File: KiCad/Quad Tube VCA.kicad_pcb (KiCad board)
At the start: 2 copper layers, 162.6 x 100.3 mm, 226 parts, among them IC1 TL072, IC10 TL072, IC2 LM358, IC3 TL072, IC4 LM358, IC5 TL072, IC6 LM358, IC7 TL072, IC8 LM358, IC9 TL072

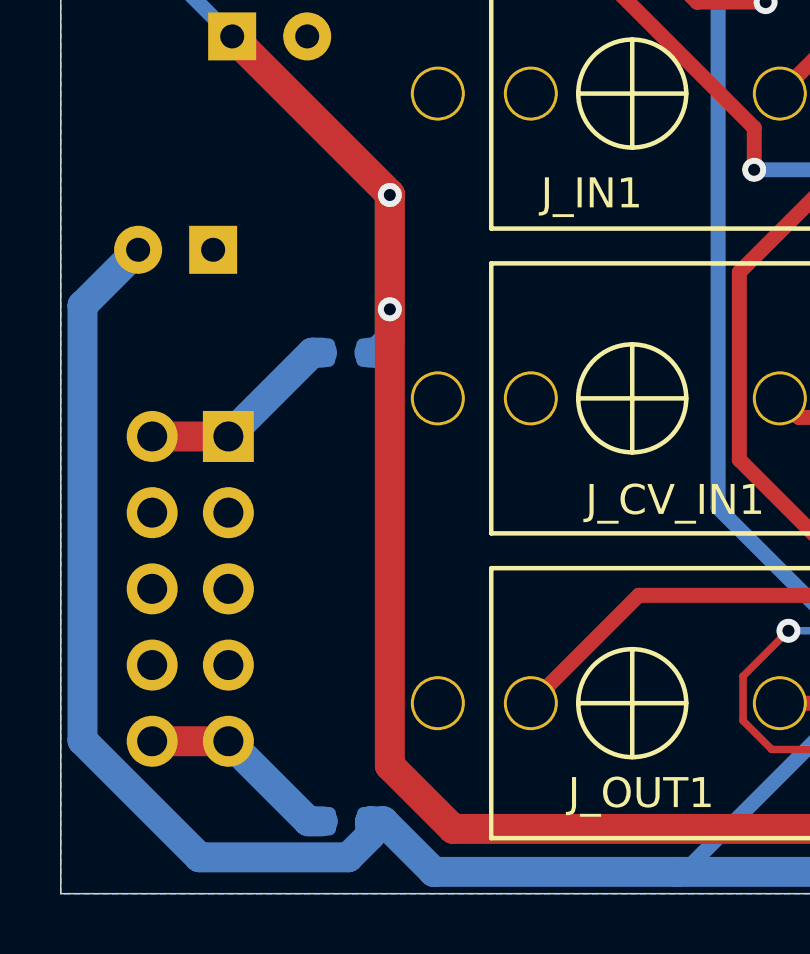
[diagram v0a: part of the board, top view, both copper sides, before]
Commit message: adds reverse power protection diodes
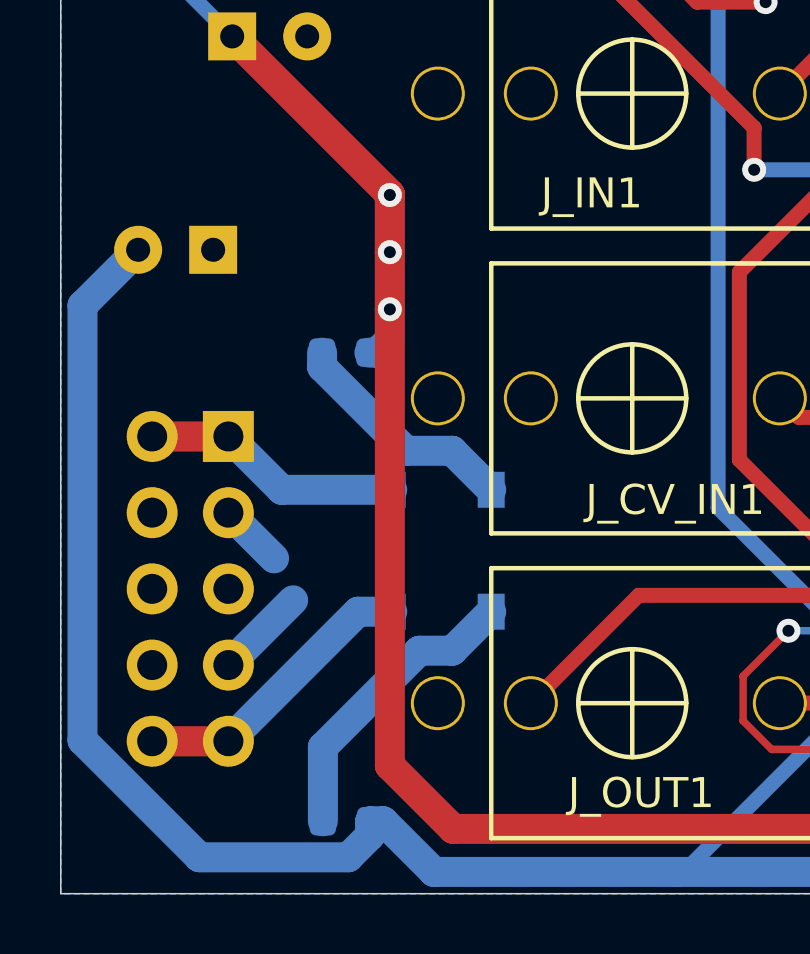
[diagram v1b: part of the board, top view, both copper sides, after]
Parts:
- added D19: 1N5819, Diode_SMD:D_SOD-123, B.Cu at (78.7, 131.3)
- added D20: 1N5819, Diode_SMD:D_SOD-123, B.Cu at (78.7, 135.4)
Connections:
- FB1 pad 1: Net-(FB1-Pad1) -> Net-(D19-Pad1)
- FB2 pad 1: Net-(FB2-Pad1) -> Net-(D20-Pad2)
- JP1 pad 1: Net-(FB1-Pad1) -> Net-(D19-Pad2)
- JP1 pad 10: Net-(FB2-Pad1) -> Net-(D20-Pad1)
- JP1 pad 2: Net-(FB1-Pad1) -> Net-(D19-Pad2)
- JP1 pad 9: Net-(FB2-Pad1) -> Net-(D20-Pad1)
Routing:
- net Net-(D20-Pad2): track 0.00 -> 9.95 mm
- net Net-(D20-Pad1): track 0.00 -> 9.79 mm
- net Net-(D19-Pad2): track 0.00 -> 8.74 mm
- net Net-(D19-Pad1): track 0.00 -> 7.81 mm
- net Net-(FB1-Pad1): track 6.82 -> 0.00 mm
- net Net-(FB2-Pad1): track 6.79 -> 0.00 mm
- net GND: track 383.2 -> 388.5 mm
- net +12V: vias 10 -> 11
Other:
- board text removed: "I’VE GOT THE POWER!!"

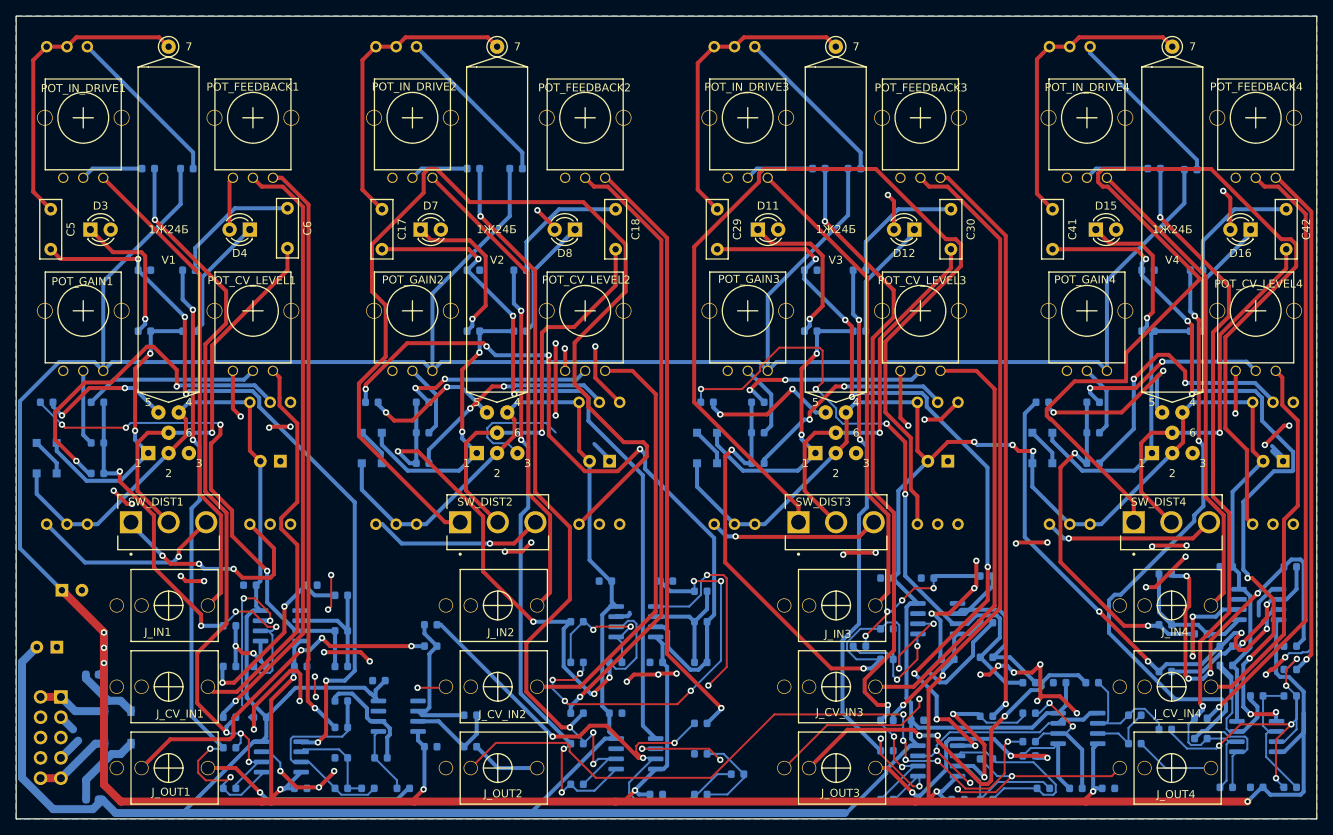
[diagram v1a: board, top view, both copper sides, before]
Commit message: removes leds from cathode/signal path
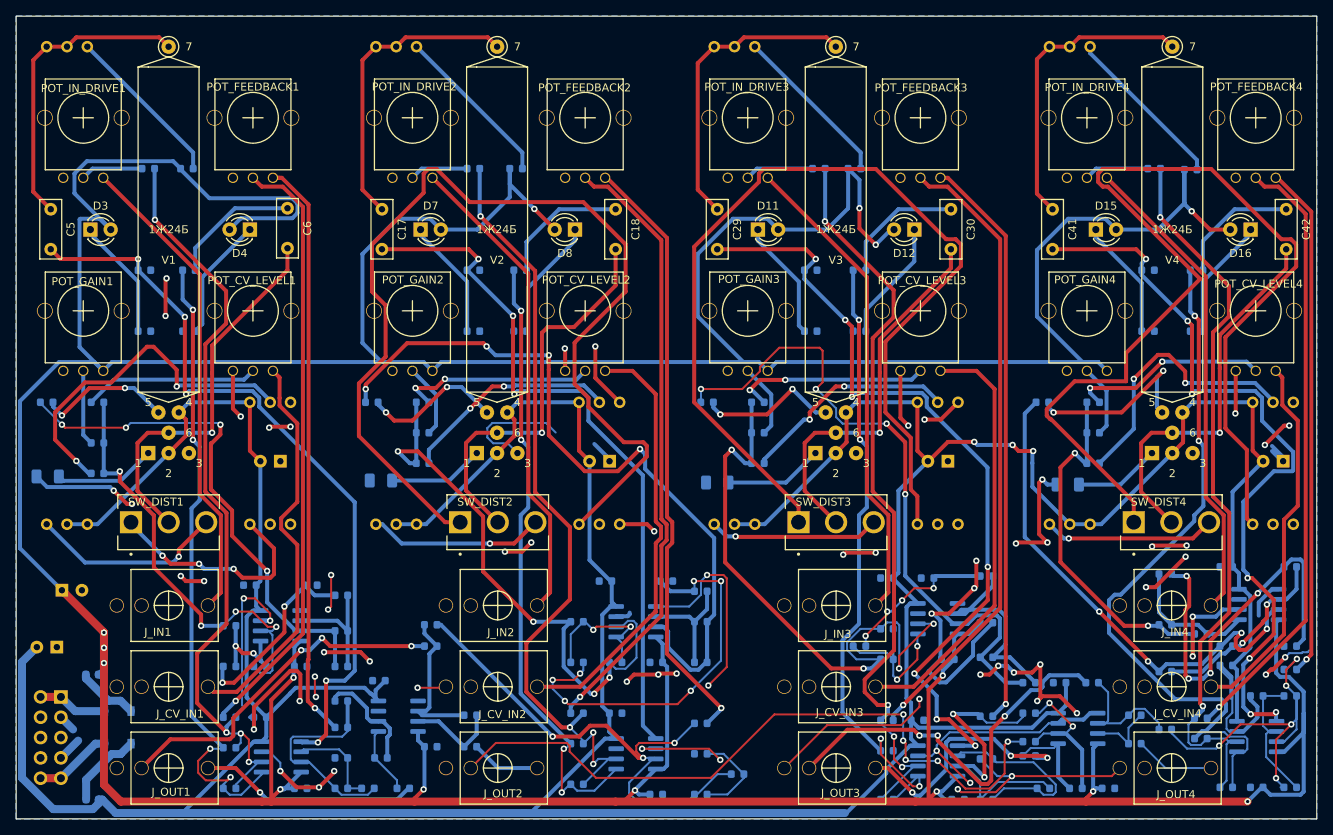
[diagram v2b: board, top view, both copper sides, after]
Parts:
- removed D10, D13, D14, D17, D18, D5, D6, D9: 1n4148, Diode_SMD:D_SOD-323_HandSoldering
- added R92: 750R, Resistor_SMD:R_1206_3216Metric, B.Cu at (70.0, 102.0)
- added R93: 750R, Resistor_SMD:R_1206_3216Metric, B.Cu at (111.6, 102.5)
- added R94: 750R, Resistor_SMD:R_1206_3216Metric, B.Cu at (153.7, 102.7)
- added R95: 750R, Resistor_SMD:R_1206_3216Metric, B.Cu at (197.5, 103.0)
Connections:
- D11 pad 2: GND -> +12V
- D12 pad 2: GND -> +12V
- D15 pad 2: GND -> +12V
- D16 pad 2: GND -> +12V
- D3 pad 2: GND -> +12V
- D4 pad 2: GND -> +12V
- D7 pad 2: GND -> +12V
- D8 pad 2: GND -> +12V
- R11 pad 1: Net-(D5-Pad2) -> GND
- R13 pad 2: Net-(D5-Pad2) -> GND
- R31 pad 1: Net-(D9-Pad2) -> GND
- R33 pad 2: Net-(D9-Pad2) -> GND
- R51 pad 1: Net-(D13-Pad2) -> GND
- R53 pad 2: Net-(D13-Pad2) -> GND
- R71 pad 1: Net-(D17-Pad2) -> GND
- R73 pad 2: Net-(D17-Pad2) -> GND
- V1 pad 1: Net-(D5-Pad2) -> Net-(R92-Pad1)
- V2 pad 1: Net-(D9-Pad2) -> Net-(R93-Pad1)
- V3 pad 1: Net-(D13-Pad2) -> Net-(R94-Pad1)
- V4 pad 1: Net-(D17-Pad2) -> Net-(R95-Pad1)
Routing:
- net +12V: track 608.9 -> 732.8 mm, vias 11 -> 15
- net Net-(D13-Pad2): track 37.3 -> 0.00 mm, vias 2 -> 0
- net Net-(D9-Pad2): track 36.8 -> 0.00 mm, vias 2 -> 0
- net Net-(D5-Pad2): track 36.2 -> 0.00 mm, vias 2 -> 0
- net Net-(D17-Pad2): track 35.8 -> 0.00 mm
- net -12V: track 571.6 -> 544.8 mm
- net Net-(R92-Pad1): track 0.00 -> 12.8 mm
- net Net-(R94-Pad1): track 0.00 -> 12.4 mm
- net Net-(R93-Pad1): track 0.00 -> 12.0 mm
- net Net-(R95-Pad1): track 0.00 -> 10.9 mm
- net Net-(D17-Pad1): track 4.85 -> 0.00 mm
- net Net-(D13-Pad1): track 4.85 -> 0.00 mm
- net Net-(D10-Pad2): track 4.85 -> 0.00 mm
- net Net-(D5-Pad1): track 4.85 -> 0.00 mm
- net Net-(D7-Pad1): track 19.8 -> 15.1 mm, vias 1 -> 0
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
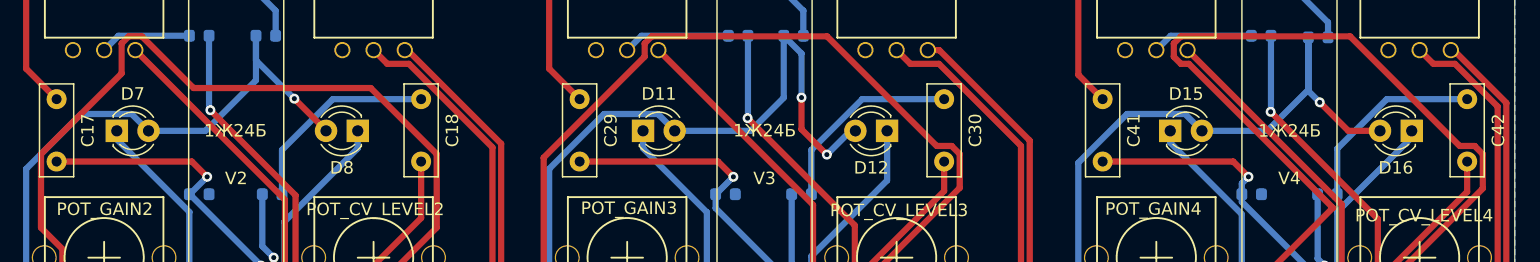
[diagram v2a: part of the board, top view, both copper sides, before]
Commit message: updates annotations - need to regen BOM
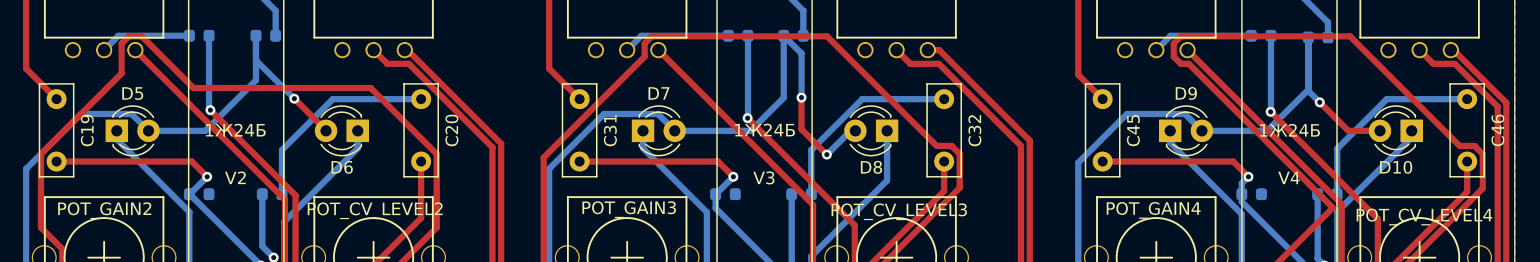
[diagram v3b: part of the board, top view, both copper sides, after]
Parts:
- renumbered C2 to C1, C51 to C10, C10 to C11, C11 to C12, C52 to C13, C12 to C14, C13 to C15, C14 to C16, C15 to C17, C16 to C18, C17 to C19, C3 to C2, C18 to C20, C19 to C21, C20 to C24, C21 to C25, C24 to C26, C25 to C27, C26 to C28, C27 to C29, C1 to C3, C28 to C30, C29 to C31, C30 to C32, C31 to C33, C32 to C34, C33 to C35, C53 to C36, C34 to C37, C35 to C38, C54 to C39, C36 to C40, C37 to C41, C38 to C42, C39 to C43, C40 to C44, C41 to C45, C42 to C46, C43 to C47, C44 to C48, C45 to C49, C46 to C50, C47 to C51, C48 to C52, C49 to C53, C50 to C54, D19 to D1, D16 to D10, D20 to D2, D7 to D5, D8 to D6, D11 to D7, D12 to D8, D15 to D9, IC8 to IC10, IC9 to IC2, IC2 to IC3, IC3 to IC4, IC4 to IC5, IC5 to IC6, IC10 to IC7, IC6 to IC8, IC7 to IC9, R8 to R10, R9 to R11, R10 to R12, R92 to R13, R12 to R14, R11 to R15, R13 to R16, R14 to R17, R15 to R18, R16 to R19, R17 to R20, R18 to R21, R19 to R22, R20 to R23, R21 to R24, R22 to R25, R23 to R26, R24 to R27, R25 to R28, R26 to R29, R85 to R30, R89 to R31, R27 to R32, R28 to R33, R82 to R34, R29 to R35, R30 to R36, R93 to R37, R31 to R38, R32 to R39, R33 to R40, R34 to R41, R35 to R42, R36 to R43, R37 to R44, R38 to R45, R39 to R46, R40 to R47, R41 to R48, R42 to R49, R43 to R50, R44 to R51, R45 to R52, R46 to R53, R86 to R54, R90 to R55, R47 to R56, R48 to R57, R83 to R58, R49 to R59, R50 to R60, R94 to R61, R52 to R62, R51 to R63, R54 to R64, R55 to R65, R53 to R66, R56 to R67, R57 to R68, R58 to R69, R88 to R7, R59 to R70, R60 to R71, R61 to R72, R62 to R73, R63 to R74, R64 to R75, R65 to R76, R66 to R77, R91 to R78, R87 to R79, R7 to R8, R67 to R80, R84 to R81, R68 to R82, R69 to R83, R70 to R84, R95 to R85, R72 to R86, R71 to R87, R74 to R88, R73 to R89, R81 to R9, R75 to R90, R76 to R91, R77 to R92, R78 to R93, R79 to R94, R80 to R95

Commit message: updates GND
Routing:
- net GND: track 390.0 -> 426.5 mm
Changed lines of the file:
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@@
     (thickness 1.6)
     (drawings 13)
-    (tracks 2015)
+    (tracks 2027)
     (zones 0)
     (modules 224)
@@
   )
   (setup
-    (last_trace_width 0.5)
+    (last_trace_width 1)
     (user_trace_width 0.5)
     (user_trace_width 1)
@@
     (descr "CP, Radial series, Radial, pin pitch=2.50mm, , diameter=5mm, Electrolytic Capacitor")
     (tags "CP Radial series Radial pin pitch 2.50mm  diameter 5mm Electrolytic Capacitor")
-    (fp_text reference C2 (at -4.445 0.381) (layer B.SilkS)
+    (fp_text reference C2 (at -3.048 0.254) (layer B.SilkS)
       (effects (font (size 1 1) (thickness 0.15)) (justify mirror))
     )
@@
     (tags capacitor)
     (attr smd)
-    (fp_text reference C13 (at 0 1.43) (layer B.SilkS)
+    (fp_text reference C13 (at 1.27 -1.524) (layer B.SilkS)
       (effects (font (size 1 1) (thickness 0.15)) (justify mirror))
     )
@@
     (tags resistor)
     (attr smd)
-    (fp_text reference R86 (at 0 1.43) (layer B.SilkS)
+    (fp_text reference R86 (at 1.524 1.43) (layer B.SilkS)
       (effects (font (size 1 1) (thickness 0.15)) (justify mirror))
     )
@@
   (segment (start 144.907 107.95) (end 145.796 108.839) (width 0.5) (layer F.Cu) (net 1))
   (segment (start 141.478 107.95) (end 144.907 107.95) (width 0.5) (layer F.Cu) (net 1))
+  (segment (start 69.088 134.62) (end 71.628 134.62) (width 1) (layer F.Cu) (net 1))
+  (segment (start 71.628 132.08) (end 69.088 134.62) (width 1) (layer B.Cu) (net 1))
+  (segment (start 71.628 134.62) (end 69.088 137.16) (width 1) (layer B.Cu) (net 1))
+  (segment (start 69.088 134.62) (end 73.406 134.62) (width 1) (layer B.Cu) (net 1))
+  (segment (start 71.628 137.16) (end 71.628 134.62) (width 1) (layer B.Cu) (net 1))
+  (segment (start 71.628 132.08) (end 71.628 134.62) (width 1) (layer B.Cu) (net 1))
+  (segment (start 69.088 132.08) (end 69.088 134.62) (width 1) (layer B.Cu) (net 1))
+  (segment (start 69.088 134.62) (end 69.088 137.16) (width 1) (layer B.Cu) (net 1))
+  (segment (start 69.088 137.16) (end 71.628 137.16) (width 1) (layer F.Cu) (net 1))
+  (segment (start 69.088 132.08) (end 71.628 132.08) (width 1) (layer F.Cu) (net 1))
+  (segment (start 71.628 134.62) (end 69.088 132.08) (width 1) (layer F.Cu) (net 1))
+  (segment (start 71.628 137.16) (end 69.088 134.62) (width 1) (layer F.Cu) (net 1))
   (segment (start 120.117501 87.679999) (end 119.170001 87.679999) (width 0.5) (layer B.Cu) (net 2))
   (segment (start 78.995001 87.679999) (end 78.022001 87.679999) (width 0.5) (layer B.Cu) (net 2))

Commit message: updates BOM
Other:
- board text added: "Vālvs v1.01 PCB Design: Olly Berry"
- board text removed: "Vālvs v1.0 PCB Design: Olly Berry"
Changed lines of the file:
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@@
   )
   (setup
-    (last_trace_width 1)
+    (last_trace_width 0.5)
     (user_trace_width 0.5)
     (user_trace_width 1)
@@
     (effects (font (size 0.4 0.6) (thickness 0.1)) (justify mirror))
   )
-  (gr_text "Vālvs v1.0\nPCB Design: Olly Berry" (at 215.011 60.579) (layer B.SilkS)
+  (gr_text "Vālvs v1.01\nPCB Design: Olly Berry" (at 215.011 60.579) (layer B.SilkS)
     (effects (font (size 1 1) (thickness 0.15)) (justify mirror))
   )
@@
   (segment (start 227.930011 68.880046) (end 223.699965 64.65) (width 0.5) (layer F.Cu) (net 82))
   (segment (start 227.33 124.841) (end 227.930011 124.240989) (width 0.5) (layer F.Cu) (net 82))
-  (segment (start 71.628 129.54) (end 69.088 129.54) (width 1) (layer F.Cu) (net 106))
   (segment (start 73.406 131.318) (end 71.628 129.54) (width 1) (layer B.Cu) (net 106))
   (segment (start 77.09 131.318) (end 73.406 131.318) (width 1) (layer B.Cu) (net 106))
+  (segment (start 71.628 129.54) (end 69.088 129.54) (width 1) (layer F.Cu) (net 106))
   (segment (start 77.548999 130.017999) (end 74.752 127.221) (width 1) (layer B.Cu) (net 107))
   (segment (start 79.089999 130.017999) (end 77.548999 130.017999) (width 1) (layer B.Cu) (net 107))
@@
   (segment (start 79.089999 136.682001) (end 77.989997 136.682001) (width 1) (layer B.Cu) (net 108))
   (segment (start 80.39 135.382) (end 79.089999 136.682001) (width 1) (layer B.Cu) (net 108))
-  (segment (start 71.628 139.7) (end 69.088 139.7) (width 1) (layer F.Cu) (net 109))
   (segment (start 75.946 135.382) (end 71.628 139.7) (width 1) (layer B.Cu) (net 109))
   (segment (start 77.09 135.382) (end 75.946 135.382) (width 1) (layer B.Cu) (net 109))
+  (segment (start 71.628 139.7) (end 69.088 139.7) (width 1) (layer F.Cu) (net 109))
   (segment (start 71.92101 102.52501) (end 79.08499 102.52501) (width 0.5) (layer B.Cu) (net 121))
   (segment (start 79.08499 102.52501) (end 82.55 99.06) (width 0.5) (layer B.Cu) (net 121))
